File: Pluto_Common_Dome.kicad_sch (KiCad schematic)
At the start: 45 parts

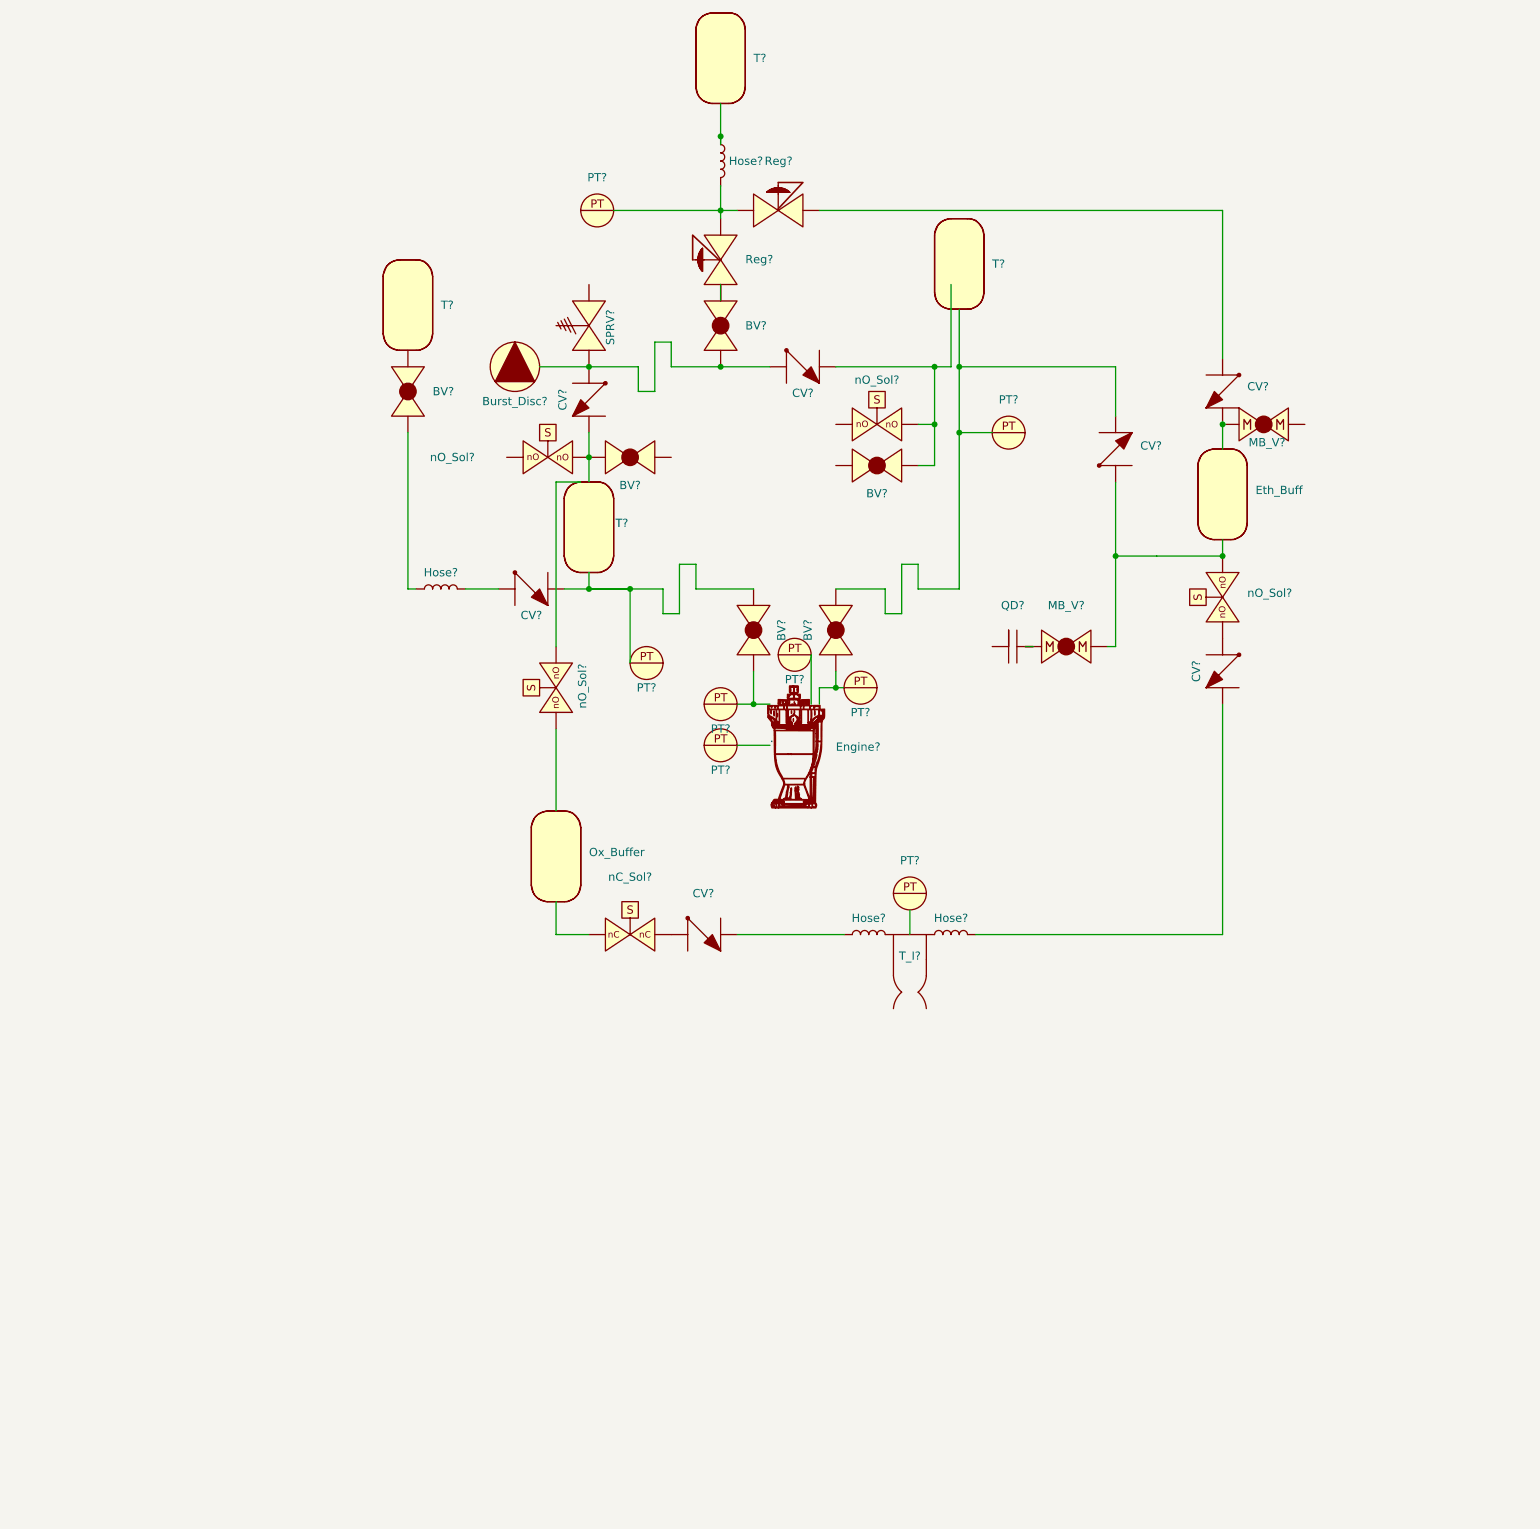
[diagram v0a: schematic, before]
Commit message: Added Pluto gss and Pluto common dome
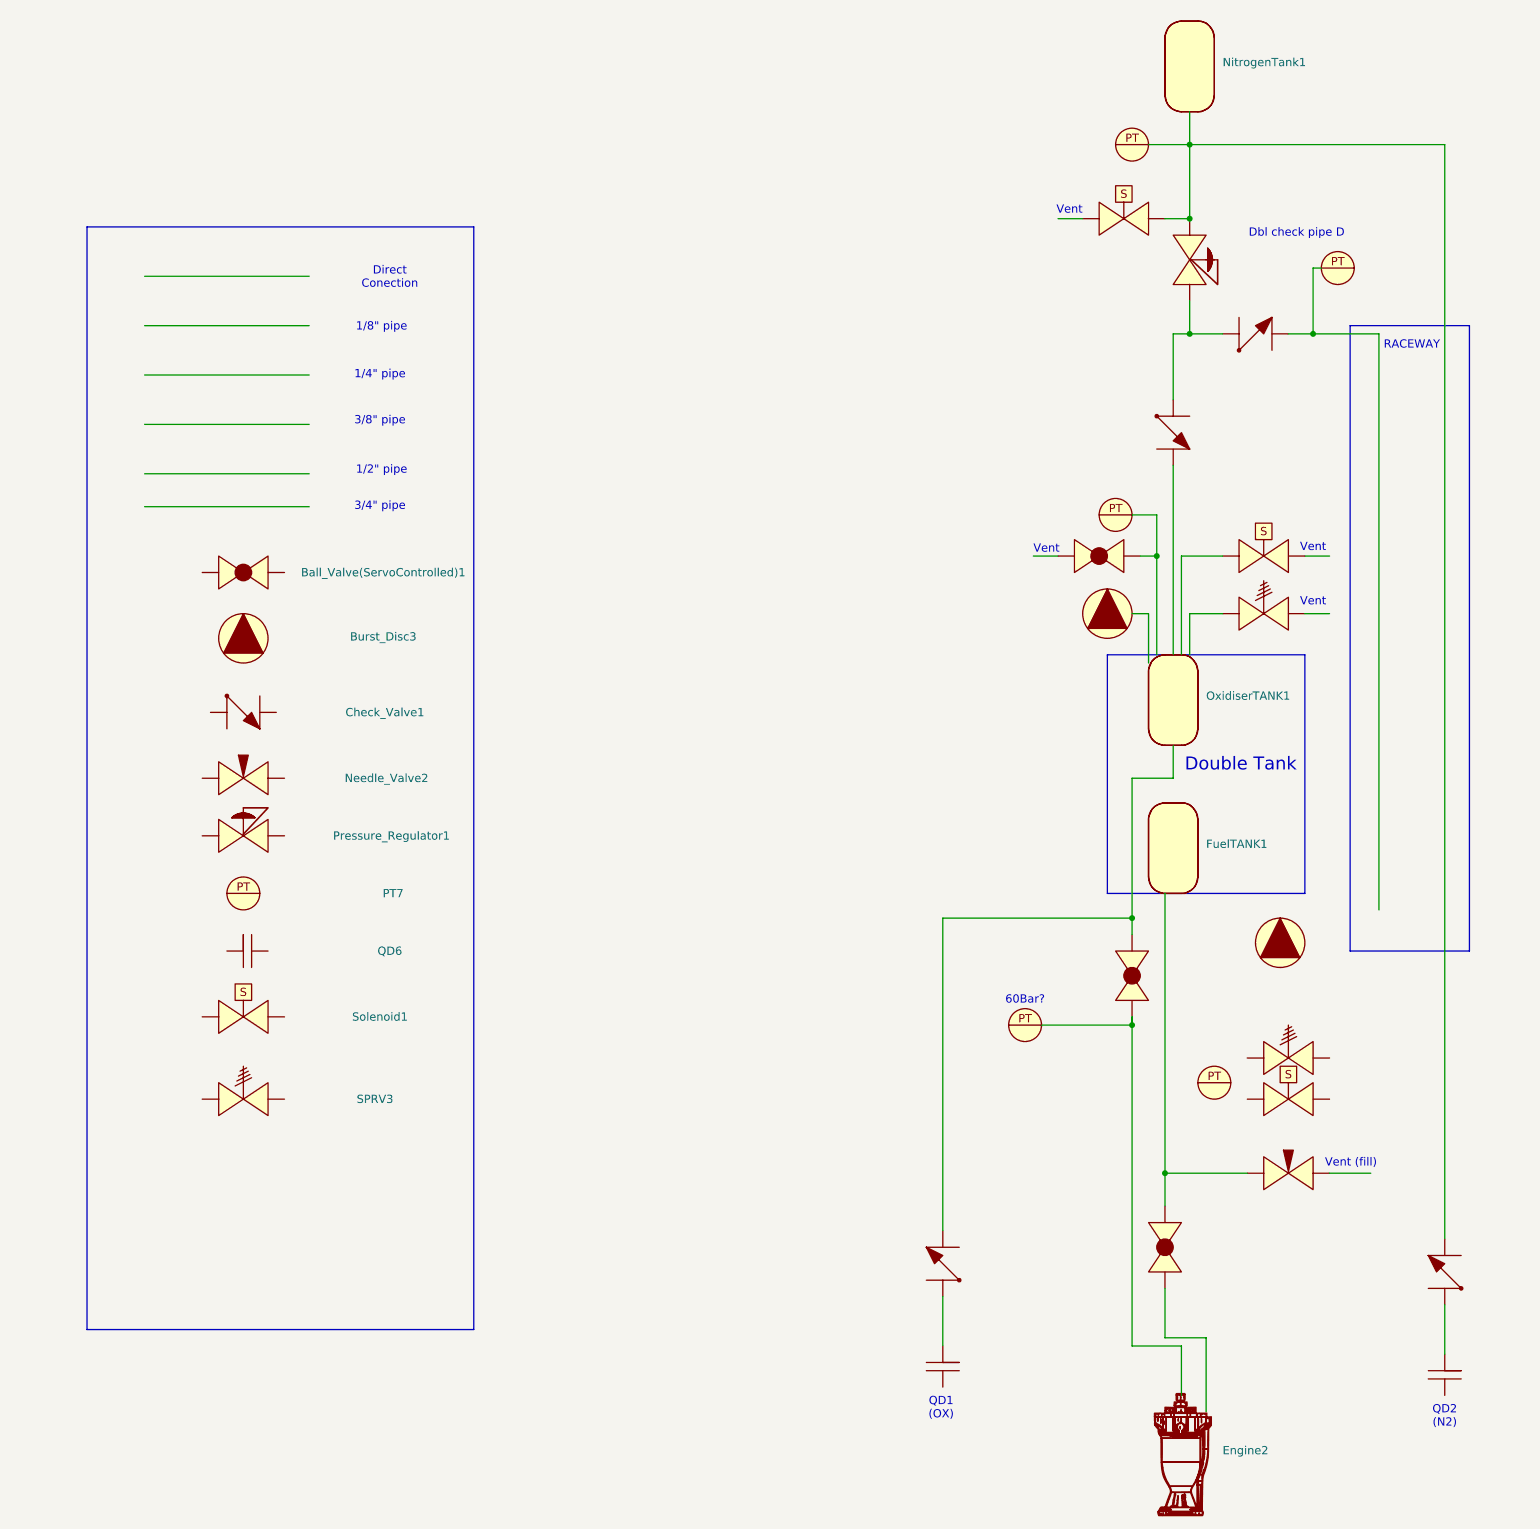
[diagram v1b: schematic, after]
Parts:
- removed BV? (x6): ~, symbol PID_symbols:Ball_Valve
- removed Burst_Disc?: ~, symbol PID_symbols:Burst_Disc
- removed CV? (x7): ~, symbol PID_symbols:Check_Valve
- removed Engine?: ~, symbol PID_symbols:Engine
- removed Eth_Buff, Ox_Buffer, T? (x4): ~, symbol PID_symbols:Tank
- removed Hose? (x4): ~, symbol Device:Hose
- removed MB_V? (x2): ~, symbol PID_symbols:MBallValve
- removed PT? (x8): ~, symbol PID_symbols:Pressure_Transducer
- removed QD?: ~, symbol PID_symbols:Quick_Disconnect
- removed Reg? (x2): ~, symbol PID_symbols:Pressure_Regulator
- removed SPRV?: ~, symbol PID_symbols:SPRV
- removed T_I?: ~, symbol Analog_ADC:Torch_Igniter
- removed nC_Sol?: ~, symbol PID_symbols:Normally_Closed_Solenoid
- removed nO_Sol? (x3): ~, symbol PID_symbols:Solenoid
- removed nO_Sol?: ~, symbol PID_symbols:Normally Open Solenoid
- added Ball_Valve(ServoControlled)1, Ball_Valve1, Ball_Valve2, Ball_Valve3: ~, symbol PID_symbols:Ball_Valve
- added Burst_Disc3, Burst_Disc4, Burst_Disc5: ~, symbol PID_symbols:Burst_Disc
- added Check_Valve1, Check_Valve2, Check_Valve3, Check_Valve4, Check_Valve5: ~, symbol PID_symbols:Check_Valve
- added Engine2: ~, symbol PID_symbols:Engine
- added FuelTANK1, NitrogenTank1, OxidiserTANK1: ~, symbol PID_symbols:Tank
- added Needle_Valve2, Needle_Valve3: ~, symbol PID_symbols:Needle_Valve
- added PT10, PT11, PT13, PT14, PT7, PT9: ~, symbol PID_symbols:Pressure_Transducer
- added Pressure_Regulator1, Pressure_Regulator2: ~, symbol PID_symbols:Pressure_Regulator
- added QD6, QD7, QD8: ~, symbol PID_symbols:Quick_Disconnect
- added SPRV3, SPRV4, SPRV5: ~, symbol PID_symbols:SPRV
- added Solenoid1, Solenoid2, Solenoid3, Solenoid4: ~, symbol PID_symbols:Solenoid
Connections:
- new net: Ball_Valve2., Engine2., PT9.
- new net: Ball_Valve2., Check_Valve2., OxidiserTANK1.
- new net: Ball_Valve3., Engine2.
- new net: Ball_Valve3., Needle_Valve3.
- new net: Check_Valve2., QD7.
- new net: Check_Valve3., Check_Valve4., Pressure_Regulator2.
- new net: Check_Valve5., NitrogenTank1., PT11., Pressure_Regulator2., Solenoid2.
- new net: Check_Valve4., PT14.
- new net: Check_Valve3., OxidiserTANK1.
- new net: Ball_Valve1., PT10.
- new net: Check_Valve5., QD8.
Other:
- note added: "1/2" pipe"
- note added: "1/4" pipe"
- note added: "1/8" pipe"
- note added: "3/4" pipe"
- note added: "3/8" pipe"
- note added: "60Bar?"
- note added: "Dbl check pipe D"
- note added: "Direct Conection"
- note added: "Double Tank"
- note added: "QD1 (OX)"
- note added: "QD2 (N2)"
- note added: "RACEWAY"
- note added: "Vent"
- note added: "Vent (fill)"
- company: (none) -> ICLR
- title: (none) -> Pluto Common Dome P&ID

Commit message: Big Pluto Commit, baboucarr jeng imperial college london second year aeronautics student.
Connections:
- net at PT9.: now also Ball_Valve2., Engine2.
- net at Ball_Valve3.: now also Needle_Valve3.; no longer Engine2.
- net at Needle_Valve3.: no longer Ball_Valve3.
- net at PT14.: now also Check_Valve4.
- net at Ball_Valve1.: now also PT10.
- net at PT10.: no longer Ball_Valve1.
- new net: Ball_Valve2., Check_Valve2., OxidiserTANK1.
- new net: Ball_Valve3., Engine2.
- new net: Check_Valve3., Check_Valve4., Pressure_Regulator2.
- new net: Check_Valve5., NitrogenTank1., PT11., Pressure_Regulator2., Solenoid2.
- now unconnected: Engine2., NitrogenTank1., PT11., Solenoid2.
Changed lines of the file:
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@@
 		(instances
 			(project "P_IDs"
-				(path "/045f1f05-3134-4b6d-91b6-463031104f1e/7d4466f7-7ed7-495d-8022-a39b57490c7d"
+				(path "/045f1f05-3134-4b6d-91b6-463031104f1e/561f91da-59dd-4c39-b4eb-a17d4e7f8654"
 					(reference "Solenoid4")
 					(unit 1)
@@
 		(instances
 			(project "P_IDs"
-				(path "/045f1f05-3134-4b6d-91b6-463031104f1e/7d4466f7-7ed7-495d-8022-a39b57490c7d"
+				(path "/045f1f05-3134-4b6d-91b6-463031104f1e/561f91da-59dd-4c39-b4eb-a17d4e7f8654"
 					(reference "PT9")
 					(unit 1)
@@
 		(instances
 			(project "P_IDs"
-				(path "/045f1f05-3134-4b6d-91b6-463031104f1e/7d4466f7-7ed7-495d-8022-a39b57490c7d"
+				(path "/045f1f05-3134-4b6d-91b6-463031104f1e/561f91da-59dd-4c39-b4eb-a17d4e7f8654"
 					(reference "Solenoid3")
 					(unit 1)
@@
 		(instances
 			(project "P_IDs"
-				(path "/045f1f05-3134-4b6d-91b6-463031104f1e/7d4466f7-7ed7-495d-8022-a39b57490c7d"
+				(path "/045f1f05-3134-4b6d-91b6-463031104f1e/561f91da-59dd-4c39-b4eb-a17d4e7f8654"
 					(reference "Ball_Valve2")
 					(unit 1)
@@
 		(instances
 			(project "P_IDs"
-				(path "/045f1f05-3134-4b6d-91b6-463031104f1e/7d4466f7-7ed7-495d-8022-a39b57490c7d"
+				(path "/045f1f05-3134-4b6d-91b6-463031104f1e/561f91da-59dd-4c39-b4eb-a17d4e7f8654"
 					(reference "Pressure_Regulator1")
 					(unit 1)
@@
 		(instances
 			(project "P_IDs"
-				(path "/045f1f05-3134-4b6d-91b6-463031104f1e/7d4466f7-7ed7-495d-8022-a39b57490c7d"
+				(path "/045f1f05-3134-4b6d-91b6-463031104f1e/561f91da-59dd-4c39-b4eb-a17d4e7f8654"
 					(reference "FuelTANK1")
 					(unit 1)
@@
 		(instances
 			(project "P_IDs"
-				(path "/045f1f05-3134-4b6d-91b6-463031104f1e/7d4466f7-7ed7-495d-8022-a39b57490c7d"
+				(path "/045f1f05-3134-4b6d-91b6-463031104f1e/561f91da-59dd-4c39-b4eb-a17d4e7f8654"
 					(reference "SPRV3")
 					(unit 1)
@@
 		(instances
 			(project "P_IDs"
-				(path "/045f1f05-3134-4b6d-91b6-463031104f1e/7d4466f7-7ed7-495d-8022-a39b57490c7d"
+				(path "/045f1f05-3134-4b6d-91b6-463031104f1e/561f91da-59dd-4c39-b4eb-a17d4e7f8654"
 					(reference "Ball_Valve3")
 					(unit 1)
@@
 		(instances
 			(project "P_IDs"
-				(path "/045f1f05-3134-4b6d-91b6-463031104f1e/7d4466f7-7ed7-495d-8022-a39b57490c7d"
+				(path "/045f1f05-3134-4b6d-91b6-463031104f1e/561f91da-59dd-4c39-b4eb-a17d4e7f8654"
 					(reference "Check_Valve2")
 					(unit 1)
@@
 		(instances
 			(project "P_IDs"
-				(path "/045f1f05-3134-4b6d-91b6-463031104f1e/7d4466f7-7ed7-495d-8022-a39b57490c7d"
+				(path "/045f1f05-3134-4b6d-91b6-463031104f1e/561f91da-59dd-4c39-b4eb-a17d4e7f8654"
 					(reference "Pressure_Regulator2")
 					(unit 1)
@@
 		(instances
 			(project "P_IDs"
-				(path "/045f1f05-3134-4b6d-91b6-463031104f1e/7d4466f7-7ed7-495d-8022-a39b57490c7d"
+				(path "/045f1f05-3134-4b6d-91b6-463031104f1e/561f91da-59dd-4c39-b4eb-a17d4e7f8654"
 					(reference "Burst_Disc5")
 					(unit 1)
@@
 		(instances
 			(project "P_IDs"
-				(path "/045f1f05-3134-4b6d-91b6-463031104f1e/7d4466f7-7ed7-495d-8022-a39b57490c7d"
+				(path "/045f1f05-3134-4b6d-91b6-463031104f1e/561f91da-59dd-4c39-b4eb-a17d4e7f8654"
 					(reference "PT14")
 					(unit 1)
@@
 		(instances
 			(project "P_IDs"
-				(path "/045f1f05-3134-4b6d-91b6-463031104f1e/7d4466f7-7ed7-495d-8022-a39b57490c7d"
+				(path "/045f1f05-3134-4b6d-91b6-463031104f1e/561f91da-59dd-4c39-b4eb-a17d4e7f8654"
 					(reference "QD6")
 					(unit 1)
@@
 		(instances
 			(project "P_IDs"
-				(path "/045f1f05-3134-4b6d-91b6-463031104f1e/7d4466f7-7ed7-495d-8022-a39b57490c7d"
+				(path "/045f1f05-3134-4b6d-91b6-463031104f1e/561f91da-59dd-4c39-b4eb-a17d4e7f8654"
 					(reference "Needle_Valve2")
 					(unit 1)
@@
 		(instances
 			(project "P_IDs"
-				(path "/045f1f05-3134-4b6d-91b6-463031104f1e/7d4466f7-7ed7-495d-8022-a39b57490c7d"
+				(path "/045f1f05-3134-4b6d-91b6-463031104f1e/561f91da-59dd-4c39-b4eb-a17d4e7f8654"
 					(reference "Check_Valve4")
 					(unit 1)
@@
 		(instances
 			(project "P_IDs"
-				(path "/045f1f05-3134-4b6d-91b6-463031104f1e/7d4466f7-7ed7-495d-8022-a39b57490c7d"
+				(path "/045f1f05-3134-4b6d-91b6-463031104f1e/561f91da-59dd-4c39-b4eb-a17d4e7f8654"
 					(reference "PT7")
 					(unit 1)
@@
 		(instances
 			(project "P_IDs"
-				(path "/045f1f05-3134-4b6d-91b6-463031104f1e/7d4466f7-7ed7-495d-8022-a39b57490c7d"
+				(path "/045f1f05-3134-4b6d-91b6-463031104f1e/561f91da-59dd-4c39-b4eb-a17d4e7f8654"
 					(reference "Check_Valve3")
 					(unit 1)
@@
 		(instances
 			(project "P_IDs"
-				(path "/045f1f05-3134-4b6d-91b6-463031104f1e/7d4466f7-7ed7-495d-8022-a39b57490c7d"
+				(path "/045f1f05-3134-4b6d-91b6-463031104f1e/561f91da-59dd-4c39-b4eb-a17d4e7f8654"
 					(reference "Ball_Valve1")
 					(unit 1)
@@
 		(instances
 			(project "P_IDs"
-				(path "/045f1f05-3134-4b6d-91b6-463031104f1e/7d4466f7-7ed7-495d-8022-a39b57490c7d"
+				(path "/045f1f05-3134-4b6d-91b6-463031104f1e/561f91da-59dd-4c39-b4eb-a17d4e7f8654"
 					(reference "Check_Valve5")
 					(unit 1)
@@
 		(instances
 			(project "P_IDs"
-				(path "/045f1f05-3134-4b6d-91b6-463031104f1e/7d4466f7-7ed7-495d-8022-a39b57490c7d"
+				(path "/045f1f05-3134-4b6d-91b6-463031104f1e/561f91da-59dd-4c39-b4eb-a17d4e7f8654"
 					(reference "Burst_Disc4")
 					(unit 1)
@@
 		(instances
 			(project "P_IDs"
-				(path "/045f1f05-3134-4b6d-91b6-463031104f1e/7d4466f7-7ed7-495d-8022-a39b57490c7d"
+				(path "/045f1f05-3134-4b6d-91b6-463031104f1e/561f91da-59dd-4c39-b4eb-a17d4e7f8654"
 					(reference "PT11")
 					(unit 1)
@@
 		(instances
 			(project "P_IDs"
-				(path "/045f1f05-3134-4b6d-91b6-463031104f1e/7d4466f7-7ed7-495d-8022-a39b57490c7d"
+				(path "/045f1f05-3134-4b6d-91b6-463031104f1e/561f91da-59dd-4c39-b4eb-a17d4e7f8654"
 					(reference "NitrogenTank1")
 					(unit 1)
@@
 		(instances
 			(project "P_IDs"
-				(path "/045f1f05-3134-4b6d-91b6-463031104f1e/7d4466f7-7ed7-495d-8022-a39b57490c7d"
+				(path "/045f1f05-3134-4b6d-91b6-463031104f1e/561f91da-59dd-4c39-b4eb-a17d4e7f8654"
 					(reference "Engine2")
 					(unit 1)
@@
 		(instances
 			(project "P_IDs"
-				(path "/045f1f05-3134-4b6d-91b6-463031104f1e/7d4466f7-7ed7-495d-8022-a39b57490c7d"
+				(path "/045f1f05-3134-4b6d-91b6-463031104f1e/561f91da-59dd-4c39-b4eb-a17d4e7f8654"
 					(reference "QD8")
 					(unit 1)
@@
 		(instances
 			(project "P_IDs"
-				(path "/045f1f05-3134-4b6d-91b6-463031104f1e/7d4466f7-7ed7-495d-8022-a39b57490c7d"
+				(path "/045f1f05-3134-4b6d-91b6-463031104f1e/561f91da-59dd-4c39-b4eb-a17d4e7f8654"
 					(reference "Check_Valve1")
 					(unit 1)
@@
 		(instances
 			(project "P_IDs"
-				(path "/045f1f05-3134-4b6d-91b6-463031104f1e/7d4466f7-7ed7-495d-8022-a39b57490c7d"
+				(path "/045f1f05-3134-4b6d-91b6-463031104f1e/561f91da-59dd-4c39-b4eb-a17d4e7f8654"
 					(reference "Needle_Valve3")
 					(unit 1)
@@
 		(instances
 			(project "P_IDs"
-				(path "/045f1f05-3134-4b6d-91b6-463031104f1e/7d4466f7-7ed7-495d-8022-a39b57490c7d"
+				(path "/045f1f05-3134-4b6d-91b6-463031104f1e/561f91da-59dd-4c39-b4eb-a17d4e7f8654"
 					(reference "Ball_Valve(ServoControlled)1")
 					(unit 1)
@@
 		(instances
 			(project "P_IDs"
-				(path "/045f1f05-3134-4b6d-91b6-463031104f1e/7d4466f7-7ed7-495d-8022-a39b57490c7d"
+				(path "/045f1f05-3134-4b6d-91b6-463031104f1e/561f91da-59dd-4c39-b4eb-a17d4e7f8654"
 					(reference "Burst_Disc3")
 					(unit 1)
@@
 		(instances
 			(project "P_IDs"
-				(path "/045f1f05-3134-4b6d-91b6-463031104f1e/7d4466f7-7ed7-495d-8022-a39b57490c7d"
+				(path "/045f1f05-3134-4b6d-91b6-463031104f1e/561f91da-59dd-4c39-b4eb-a17d4e7f8654"
 					(reference "OxidiserTANK1")
 					(unit 1)
@@
 		(instances
 			(project "P_IDs"
-				(path "/045f1f05-3134-4b6d-91b6-463031104f1e/7d4466f7-7ed7-495d-8022-a39b57490c7d"
+				(path "/045f1f05-3134-4b6d-91b6-463031104f1e/561f91da-59dd-4c39-b4eb-a17d4e7f8654"
 					(reference "Solenoid1")
 					(unit 1)
@@
 		(instances
 			(project "P_IDs"
-				(path "/045f1f05-3134-4b6d-91b6-463031104f1e/7d4466f7-7ed7-495d-8022-a39b57490c7d"
+				(path "/045f1f05-3134-4b6d-91b6-463031104f1e/561f91da-59dd-4c39-b4eb-a17d4e7f8654"
 					(reference "PT10")
 					(unit 1)
@@
 		(instances
 			(project "P_IDs"
-				(path "/045f1f05-3134-4b6d-91b6-463031104f1e/7d4466f7-7ed7-495d-8022-a39b57490c7d"
+				(path "/045f1f05-3134-4b6d-91b6-463031104f1e/561f91da-59dd-4c39-b4eb-a17d4e7f8654"
 					(reference "QD7")
 					(unit 1)
@@
 		(instances
 			(project "P_IDs"
-				(path "/045f1f05-3134-4b6d-91b6-463031104f1e/7d4466f7-7ed7-495d-8022-a39b57490c7d"
+				(path "/045f1f05-3134-4b6d-91b6-463031104f1e/561f91da-59dd-4c39-b4eb-a17d4e7f8654"
 					(reference "SPRV5")
 					(unit 1)
@@
 		(instances
 			(project "P_IDs"
-				(path "/045f1f05-3134-4b6d-91b6-463031104f1e/7d4466f7-7ed7-495d-8022-a39b57490c7d"
+				(path "/045f1f05-3134-4b6d-91b6-463031104f1e/561f91da-59dd-4c39-b4eb-a17d4e7f8654"
 					(reference "PT13")
 					(unit 1)
@@
 		(instances
 			(project "P_IDs"
-				(path "/045f1f05-3134-4b6d-91b6-463031104f1e/7d4466f7-7ed7-495d-8022-a39b57490c7d"
+				(path "/045f1f05-3134-4b6d-91b6-463031104f1e/561f91da-59dd-4c39-b4eb-a17d4e7f8654"
 					(reference "Solenoid2")
 					(unit 1)
@@
 		(instances
 			(project "P_IDs"
-				(path "/045f1f05-3134-4b6d-91b6-463031104f1e/7d4466f7-7ed7-495d-8022-a39b57490c7d"
+				(path "/045f1f05-3134-4b6d-91b6-463031104f1e/561f91da-59dd-4c39-b4eb-a17d4e7f8654"
 					(reference "SPRV4")
 					(unit 1)
